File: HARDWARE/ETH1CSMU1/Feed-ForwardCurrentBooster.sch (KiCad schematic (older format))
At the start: 49 parts

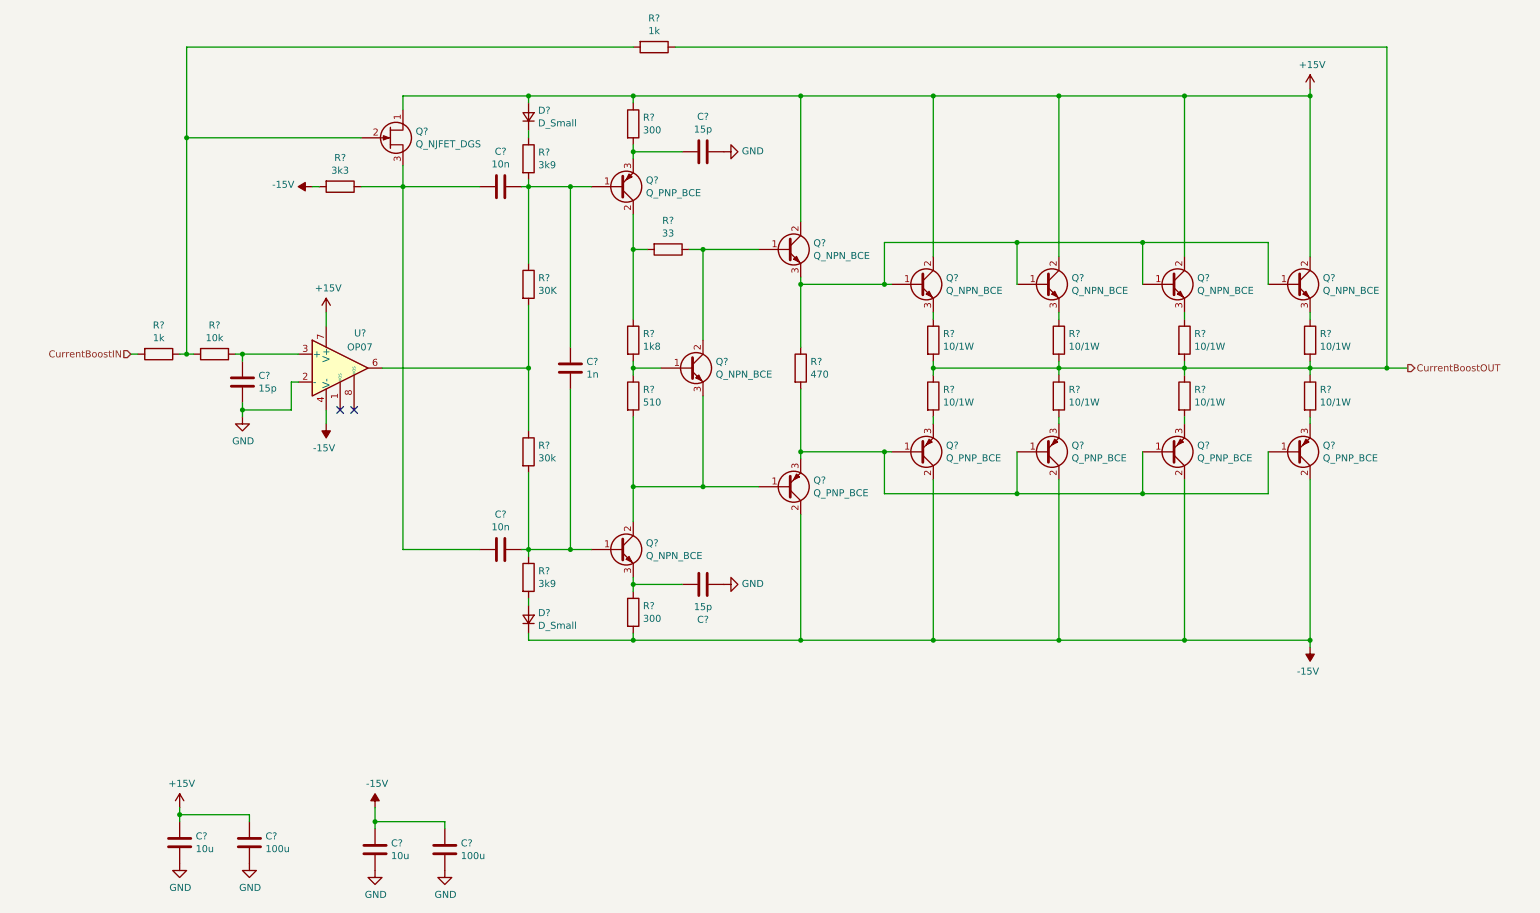
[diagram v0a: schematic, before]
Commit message: Added ADC
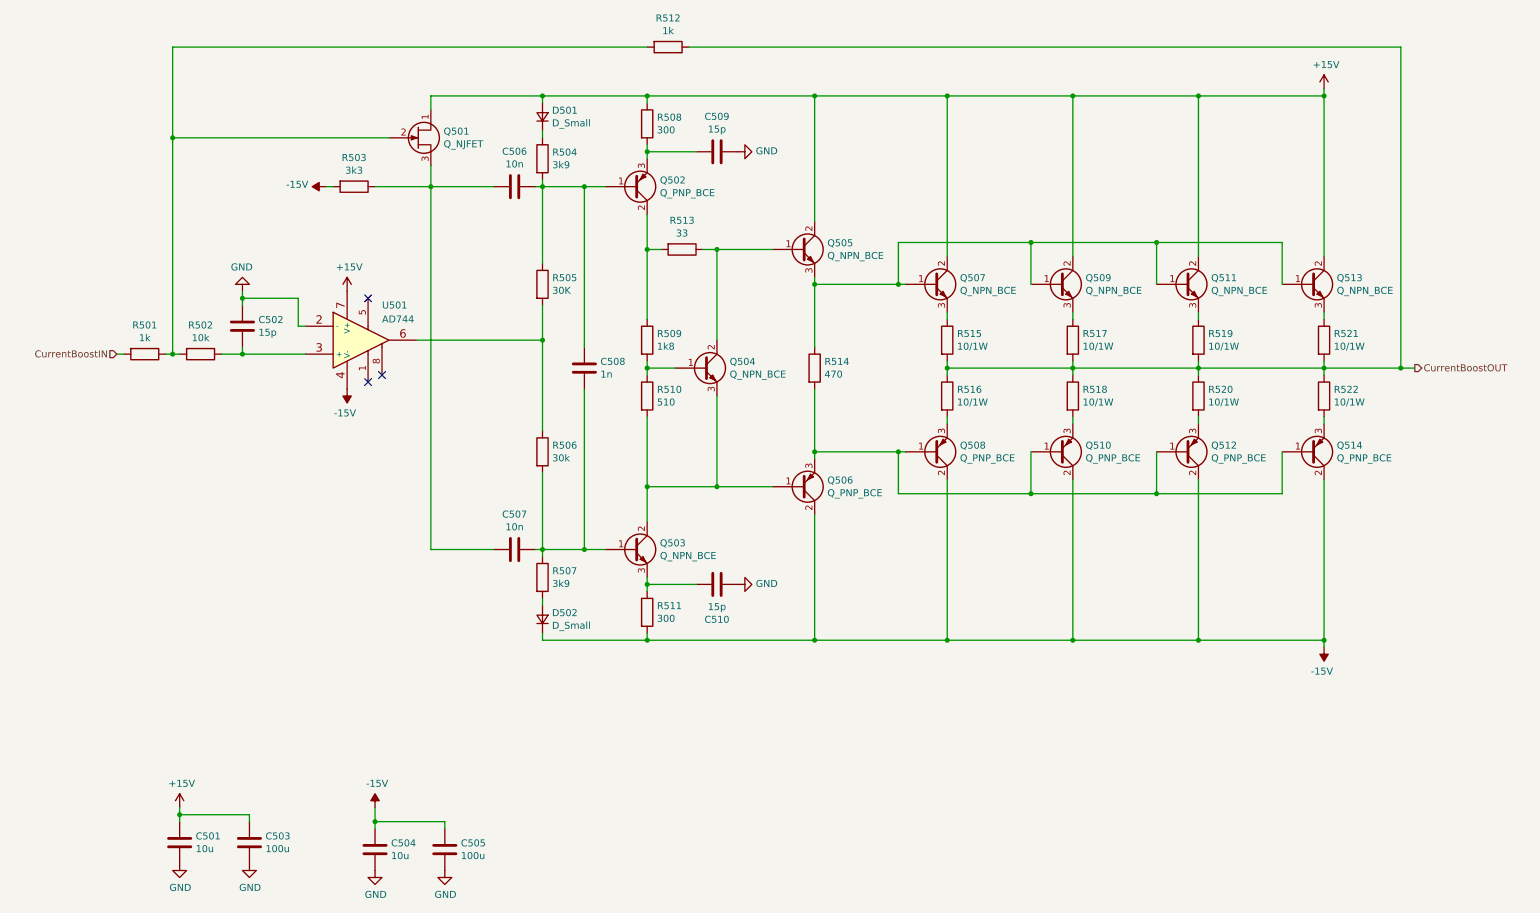
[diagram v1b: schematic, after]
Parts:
- removed U?: OP07, symbol Amplifier_Operational:OP07
- added U501: AD744, symbol opamp_local:AD744
- Q501: renamed from Q?; value Q_NJFET_DGS -> Q_NJFET
- gave numbers to parts that had none: 47
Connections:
- net +15V: now also U501.7 (V+)
- net -15V: now also U501.4 (V-)
- net GND: now also C502.1, U501.2 (-); no longer C502.2
- net at R505.2, R506.1: now also U501.6
- net at R502.1: now also C502.2, U501.3 (+); no longer C502.1
- no-connect marks 2 -> 3
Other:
- moved on the sheet: C502, C506, C507, C508, C509, C510, D501, D502, Q501, Q502, Q503, Q504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

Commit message: Commit
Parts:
- D501, D502: value D_Small -> 1N4148WS
- Q501: value Q_NJFET -> MMBF5486
- Q502, Q506: value Q_PNP_BCE -> MMBT200
- Q503, Q504, Q505: value Q_NPN_BCE -> SMBT2222
- Q507, Q509, Q511, Q513: value Q_NPN_BCE -> BCP56-16
- Q508, Q510, Q512, Q514: value Q_PNP_BCE -> BCP53
- R502: footprint (none) -> SMD:R_0603_Symbol1
- R515, R516, R517, R518, R519, R520, R521, R522: value 10/1W -> 10/2W
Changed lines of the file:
@@
 P 7100 3550
 F 0 "R515" H 7170 3596 50  0000 L CNN
-F 1 "10/1W" H 7170 3505 50  0000 L CNN
+F 1 "10/2W" H 7170 3505 50  0000 L CNN
 F 2 "" V 7030 3550 50  0001 C CNN
 F 3 "~" H 7100 3550 50  0001 C CNN
@@
 P 7100 3950
 F 0 "R516" H 7170 3996 50  0000 L CNN
-F 1 "10/1W" H 7170 3905 50  0000 L CNN
+F 1 "10/2W" H 7170 3905 50  0000 L CNN
 F 2 "" V 7030 3950 50  0001 C CNN
 F 3 "~" H 7100 3950 50  0001 C CNN
@@
 P 7000 3150
 F 0 "Q507" H 7191 3196 50  0000 L CNN
-F 1 "Q_NPN_BCE" H 7191 3105 50  0000 L CNN
+F 1 "BCP56-16" H 7191 3105 50  0000 L CNN
 F 2 "" H 7200 3250 50  0001 C CNN
 F 3 "~" H 7000 3150 50  0001 C CNN
@@
 P 6050 2900
 F 0 "Q505" H 6241 2946 50  0000 L CNN
-F 1 "Q_NPN_BCE" H 6241 2855 50  0000 L CNN
+F 1 "SMBT2222" H 6241 2855 50  0000 L CNN
 F 2 "" H 6250 3000 50  0001 C CNN
 F 3 "~" H 6050 2900 50  0001 C CNN
@@
 P 7000 4350
 F 0 "Q508" H 7191 4304 50  0000 L CNN
-F 1 "Q_PNP_BCE" H 7191 4395 50  0000 L CNN
+F 1 "BCP53" H 7191 4395 50  0000 L CNN
 F 2 "" H 7200 4450 50  0001 C CNN
 F 3 "~" H 7000 4350 50  0001 C CNN
@@
 P 6050 4600
 F 0 "Q506" H 6241 4554 50  0000 L CNN
-F 1 "Q_PNP_BCE" H 6241 4645 50  0000 L CNN
+F 1 "MMBT200" H 6241 4645 50  0000 L CNN
 F 2 "" H 6250 4700 50  0001 C CNN
 F 3 "~" H 6050 4600 50  0001 C CNN
@@
 P 5350 3750
 F 0 "Q504" H 5541 3796 50  0000 L CNN
-F 1 "Q_NPN_BCE" H 5541 3705 50  0000 L CNN
+F 1 "SMBT2222" H 5541 3705 50  0000 L CNN
 F 2 "" H 5550 3850 50  0001 C CNN
 F 3 "~" H 5350 3750 50  0001 C CNN
@@
 P 4850 5050
 F 0 "Q503" H 5041 5096 50  0000 L CNN
-F 1 "Q_NPN_BCE" H 5041 5005 50  0000 L CNN
+F 1 "SMBT2222" H 5041 5005 50  0000 L CNN
 F 2 "" H 5050 5150 50  0001 C CNN
 F 3 "~" H 4850 5050 50  0001 C CNN
@@
 P 4850 2450
 F 0 "Q502" H 5041 2404 50  0000 L CNN
-F 1 "Q_PNP_BCE" H 5041 2495 50  0000 L CNN
+F 1 "MMBT200" H 5041 2495 50  0000 L CNN
 F 2 "" H 5050 2550 50  0001 C CNN
 F 3 "~" H 4850 2450 50  0001 C CNN
@@
 P 4200 1950
 F 0 "D501" V 4246 1882 50  0000 R CNN
-F 1 "D_Small" V 4155 1882 50  0000 R CNN
+F 1 "1N4148WS" V 4155 1882 50  0000 R CNN
 F 2 "" V 4200 1950 50  0001 C CNN
 F 3 "~" V 4200 1950 50  0001 C CNN
@@
 P 4200 5550
 F 0 "D502" V 4246 5482 50  0000 R CNN
-F 1 "D_Small" V 4155 5482 50  0000 R CNN
+F 1 "1N4148WS" V 4155 5482 50  0000 R CNN
 F 2 "" V 4200 5550 50  0001 C CNN
 F 3 "~" V 4200 5550 50  0001 C CNN
@@
 P 3300 2100
 F 0 "Q501" H 3491 2146 50  0000 L CNN
-F 1 "Q_NJFET" H 3491 2055 50  0000 L CNN
+F 1 "MMBF5486" H 3491 2055 50  0000 L CNN
 F 2 "" H 3500 2200 50  0001 C CNN
 F 3 "~" H 3300 2100 50  0001 C CNN
@@
 F 0 "R502" V 1543 3650 50  0000 C CNN
 F 1 "10k" V 1634 3650 50  0000 C CNN
-F 2 "" V 1680 3650 50  0001 C CNN
+F 2 "SMD:R_0603_Symbol1" V 1680 3650 50  0001 C CNN
 F 3 "~" H 1750 3650 50  0001 C CNN
 	1    1750 3650
@@
 P 8000 3550
 F 0 "R517" H 8070 3596 50  0000 L CNN
-F 1 "10/1W" H 8070 3505 50  0000 L CNN
+F 1 "10/2W" H 8070 3505 50  0000 L CNN
 F 2 "" V 7930 3550 50  0001 C CNN
 F 3 "~" H 8000 3550 50  0001 C CNN
@@
 P 8000 3950
 F 0 "R518" H 8070 3996 50  0000 L CNN
-F 1 "10/1W" H 8070 3905 50  0000 L CNN
+F 1 "10/2W" H 8070 3905 50  0000 L CNN
 F 2 "" V 7930 3950 50  0001 C CNN
 F 3 "~" H 8000 3950 50  0001 C CNN
@@
 P 7900 3150
 F 0 "Q509" H 8091 3196 50  0000 L CNN
-F 1 "Q_NPN_BCE" H 8091 3105 50  0000 L CNN
+F 1 "BCP56-16" H 8091 3105 50  0000 L CNN
 F 2 "" H 8100 3250 50  0001 C CNN
 F 3 "~" H 7900 3150 50  0001 C CNN
@@
 P 7900 4350
 F 0 "Q510" H 8091 4304 50  0000 L CNN
-F 1 "Q_PNP_BCE" H 8091 4395 50  0000 L CNN
+F 1 "BCP53" H 8091 4395 50  0000 L CNN
 F 2 "" H 8100 4450 50  0001 C CNN
 F 3 "~" H 7900 4350 50  0001 C CNN
@@
 P 8900 3550
 F 0 "R519" H 8970 3596 50  0000 L CNN
-F 1 "10/1W" H 8970 3505 50  0000 L CNN
+F 1 "10/2W" H 8970 3505 50  0000 L CNN
 F 2 "" V 8830 3550 50  0001 C CNN
 F 3 "~" H 8900 3550 50  0001 C CNN
@@
 P 8900 3950
 F 0 "R520" H 8970 3996 50  0000 L CNN
-F 1 "10/1W" H 8970 3905 50  0000 L CNN
+F 1 "10/2W" H 8970 3905 50  0000 L CNN
 F 2 "" V 8830 3950 50  0001 C CNN
 F 3 "~" H 8900 3950 50  0001 C CNN
@@
 P 8800 3150
 F 0 "Q511" H 8991 3196 50  0000 L CNN
-F 1 "Q_NPN_BCE" H 8991 3105 50  0000 L CNN
+F 1 "BCP56-16" H 8991 3105 50  0000 L CNN
 F 2 "" H 9000 3250 50  0001 C CNN
 F 3 "~" H 8800 3150 50  0001 C CNN
@@
 P 8800 4350
 F 0 "Q512" H 8991 4304 50  0000 L CNN
-F 1 "Q_PNP_BCE" H 8991 4395 50  0000 L CNN
+F 1 "BCP53" H 8991 4395 50  0000 L CNN
 F 2 "" H 9000 4450 50  0001 C CNN
 F 3 "~" H 8800 4350 50  0001 C CNN
@@
 P 9800 3550
 F 0 "R521" H 9870 3596 50  0000 L CNN
-F 1 "10/1W" H 9870 3505 50  0000 L CNN
+F 1 "10/2W" H 9870 3505 50  0000 L CNN
 F 2 "" V 9730 3550 50  0001 C CNN
 F 3 "~" H 9800 3550 50  0001 C CNN
@@
 P 9800 3950
 F 0 "R522" H 9870 3996 50  0000 L CNN
-F 1 "10/1W" H 9870 3905 50  0000 L CNN
+F 1 "10/2W" H 9870 3905 50  0000 L CNN
 F 2 "" V 9730 3950 50  0001 C CNN
 F 3 "~" H 9800 3950 50  0001 C CNN
@@
 P 9700 3150
 F 0 "Q513" H 9891 3196 50  0000 L CNN
-F 1 "Q_NPN_BCE" H 9891 3105 50  0000 L CNN
+F 1 "BCP56-16" H 9891 3105 50  0000 L CNN
 F 2 "" H 9900 3250 50  0001 C CNN
 F 3 "~" H 9700 3150 50  0001 C CNN
@@
 P 9700 4350
 F 0 "Q514" H 9891 4304 50  0000 L CNN
-F 1 "Q_PNP_BCE" H 9891 4395 50  0000 L CNN
+F 1 "BCP53" H 9891 4395 50  0000 L CNN
 F 2 "" H 9900 4450 50  0001 C CNN
 F 3 "~" H 9700 4350 50  0001 C CNN
@@
 F 0 "U501" H 3050 3800 50  0000 L CNN
 F 1 "AD744" H 3050 3700 50  0000 L CNN
-F 2 "" H 2900 3550 60  0000 C CNN
+F 2 "" H 2900 3550 60  0001 C CNN
 F 3 "" H 2900 3550 60  0000 C CNN
 	1    2800 3550

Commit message: Footprints
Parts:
- removed C503, C505: 100u, symbol Device:C
- added C503, C505: 100u, symbol Device:CP
- C502, C509, C510: footprint (none) -> SMD:C_0603_Symbol5
- C506, C507: footprint (none) -> SMD:C_0603_Symbol2
- C508: footprint (none) -> Capacitors_SMD:C_0603
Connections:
- net +15V: now also C503.1
- net -15V: now also C505.2
- net GND: now also C503.2, C505.1
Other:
- moved on the sheet: C501
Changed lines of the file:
@@
 F 0 "C508" H 4615 3796 50  0000 L CNN
 F 1 "1n" H 4615 3705 50  0000 L CNN
-F 2 "" H 4538 3600 50  0001 C CNN
+F 2 "Capacitors_SMD:C_0603" H 4538 3600 50  0001 C CNN
 F 3 "~" H 4500 3750 50  0001 C CNN
 	1    4500 3750
@@
 F 0 "C509" V 5198 2200 50  0000 C CNN
 F 1 "15p" V 5289 2200 50  0000 C CNN
-F 2 "" H 5488 2050 50  0001 C CNN
+F 2 "SMD:C_0603_Symbol5" H 5488 2050 50  0001 C CNN
 F 3 "~" H 5450 2200 50  0001 C CNN
 	1    5450 2200
@@
 F 0 "C510" V 5198 5300 50  0000 C CNN
 F 1 "15p" V 5289 5300 50  0000 C CNN
-F 2 "" H 5488 5150 50  0001 C CNN
+F 2 "SMD:C_0603_Symbol5" H 5488 5150 50  0001 C CNN
 F 3 "~" H 5450 5300 50  0001 C CNN
 	1    5450 5300
@@
 F 0 "C507" V 3748 5050 50  0000 C CNN
 F 1 "10n" V 3839 5050 50  0000 C CNN
-F 2 "" H 4038 4900 50  0001 C CNN
+F 2 "SMD:C_0603_Symbol2" H 4038 4900 50  0001 C CNN
 F 3 "~" H 4000 5050 50  0001 C CNN
 	1    4000 5050
@@
 F 0 "C506" V 3748 2450 50  0000 C CNN
 F 1 "10n" V 3839 2450 50  0000 C CNN
-F 2 "" H 4038 2300 50  0001 C CNN
+F 2 "SMD:C_0603_Symbol2" H 4038 2300 50  0001 C CNN
 F 3 "~" H 4000 2450 50  0001 C CNN
 	1    4000 2450
@@
 L Device:C C501
 U 1 1 5BDC1227
-P 1600 7150
-F 0 "C501" H 1715 7196 50  0000 L CNN
-F 1 "10u" H 1715 7105 50  0000 L CNN
-F 2 "" H 1638 7000 50  0001 C CNN
-F 3 "~" H 1600 7150 50  0001 C CNN
-	1    1600 7150
-	1    0    0    -1
-$EndComp
-Wire Wire Line
-	1600 7000 1600 6950
+P 1600 7200
+F 0 "C501" H 1715 7246 50  0000 L CNN
+F 1 "10u" H 1715 7155 50  0000 L CNN
+F 2 "" H 1638 7050 50  0001 C CNN
+F 3 "~" H 1600 7200 50  0001 C CNN
+	1    1600 7200
+	1    0    0    -1
+$EndComp
+Wire Wire Line
+	1600 7050 1600 7000
 $Comp
 L power:GND #PWR0502
 U 1 1 5BDC3348
-P 1600 7300
-F 0 "#PWR0502" H 1600 7050 50  0001 C CNN
-F 1 "GND" H 1605 7127 50  0000 C CNN
-F 2 "" H 1600 7300 50  0001 C CNN
-F 3 "" H 1600 7300 50  0001 C CNN
-	1    1600 7300
-	1    0    0    -1
-$EndComp
-$Comp
-L Device:C C503
-U 1 1 5BDC38B6
-P 2100 7150
-F 0 "C503" H 2215 7196 50  0000 L CNN
-F 1 "100u" H 2215 7105 50  0000 L CNN
-F 2 "" H 2138 7000 50  0001 C CNN
-F 3 "~" H 2100 7150 50  0001 C CNN
-	1    2100 7150
+P 1600 7350
+F 0 "#PWR0502" H 1600 7100 50  0001 C CNN
+F 1 "GND" H 1605 7177 50  0000 C CNN
+F 2 "" H 1600 7350 50  0001 C CNN
+F 3 "" H 1600 7350 50  0001 C CNN
+	1    1600 7350
 	1    0    0    -1
 $EndComp
@@
 L power:GND #PWR0504
 U 1 1 5BDC3E2C
-P 2100 7300
-F 0 "#PWR0504" H 2100 7050 50  0001 C CNN
-F 1 "GND" H 2105 7127 50  0000 C CNN
-F 2 "" H 2100 7300 50  0001 C CNN
-F 3 "" H 2100 7300 50  0001 C CNN
-	1    2100 7300
-	1    0    0    -1
-$EndComp
-Wire Wire Line
-	2100 7000 2100 6950
-Wire Wire Line
-	2100 6950 1600 6950
+P 2100 7350
+F 0 "#PWR0504" H 2100 7100 50  0001 C CNN
+F 1 "GND" H 2105 7177 50  0000 C CNN
+F 2 "" H 2100 7350 50  0001 C CNN
+F 3 "" H 2100 7350 50  0001 C CNN
+	1    2100 7350
+	1    0    0    -1
+$EndComp
+Wire Wire Line
+	2100 7050 2100 7000
+Wire Wire Line
+	2100 7000 1600 7000
 $Comp
 L Device:C C504
@@
 F 3 "" H 3000 7350 50  0001 C CNN
 	1    3000 7350
-	1    0    0    -1
-$EndComp
-$Comp
-L Device:C C505
-U 1 1 5BDC638B
-P 3500 7200
-F 0 "C505" H 3615 7246 50  0000 L CNN
-F 1 "100u" H 3615 7155 50  0000 L CNN
-F 2 "" H 3538 7050 50  0001 C CNN
-F 3 "~" H 3500 7200 50  0001 C CNN
-	1    3500 7200
 	1    0    0    -1
 $EndComp
@@
 F 0 "C502" H 2165 3496 50  0000 L CNN
 F 1 "15p" H 2165 3405 50  0000 L CNN
-F 2 "" H 2088 3300 50  0001 C CNN
+F 2 "SMD:C_0603_Symbol5" H 2088 3300 50  0001 C CNN
 F 3 "~" H 2050 3450 50  0001 C CNN
 	1    2050 3450
@@
 L power:+15V #PWR0501
 U 1 1 5BE3B4B4
-P 1600 6900
-F 0 "#PWR0501" H 1600 6750 50  0001 C CNN
-F 1 "+15V" H 1615 7073 50  0000 C CNN
-F 2 "" H 1600 6900 50  0001 C CNN
-F 3 "" H 1600 6900 50  0001 C CNN
-	1    1600 6900
+P 1600 6950
+F 0 "#PWR0501" H 1600 6800 50  0001 C CNN
+F 1 "+15V" H 1615 7123 50  0000 C CNN
+F 2 "" H 1600 6950 50  0001 C CNN
+F 3 "" H 1600 6950 50  0001 C CNN
+	1    1600 6950
 	1    0    0    -1
 $EndComp
@@
 $EndComp
 Wire Wire Line
-	1600 6900 1600 6950
-Connection ~ 1600 6950
+	1600 6950 1600 7000
+Connection ~ 1600 7000
 Wire Wire Line
 	3000 6900 3000 7000
@@
 Wire Wire Line
 	1900 3650 2050 3650
+$Comp
+L Device:CP C503
+U 1 1 5C806E1C
+P 2100 7200
+F 0 "C503" H 2218 7246 50  0000 L CNN
+F 1 "100u" H 2218 7155 50  0000 L CNN
+F 2 "" H 2138 7050 50  0001 C CNN
+F 3 "~" H 2100 7200 50  0001 C CNN
+	1    2100 7200
+	1    0    0    -1
+$EndComp
+$Comp
+L Device:CP C505
+U 1 1 5C809259
+P 3500 7200
+F 0 "C505" H 3382 7154 50  0000 R CNN
+F 1 "100u" H 3382 7245 50  0000 R CNN
+F 2 "" H 3538 7050 50  0001 C CNN
+F 3 "~" H 3500 7200 50  0001 C CNN
+	1    3500 7200
+	-1   0    0    1
+$EndComp
 $EndSCHEMATC

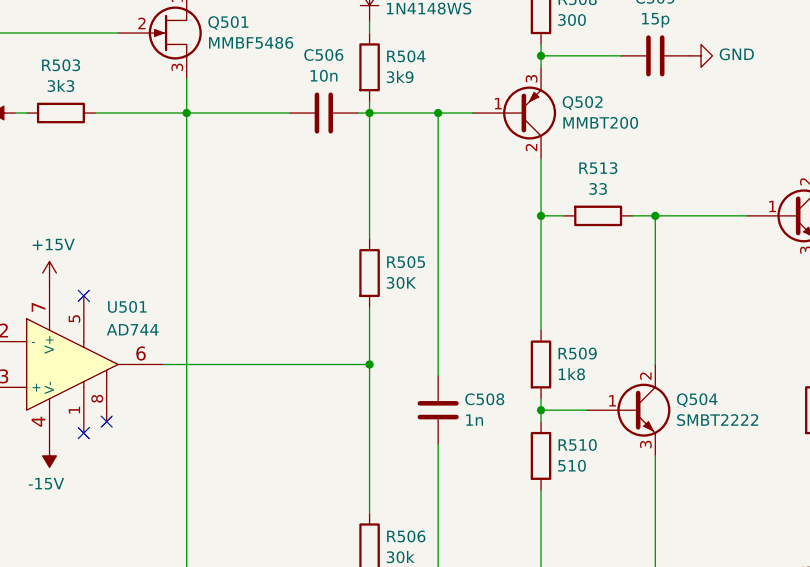
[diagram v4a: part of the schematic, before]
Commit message: Footprint selection
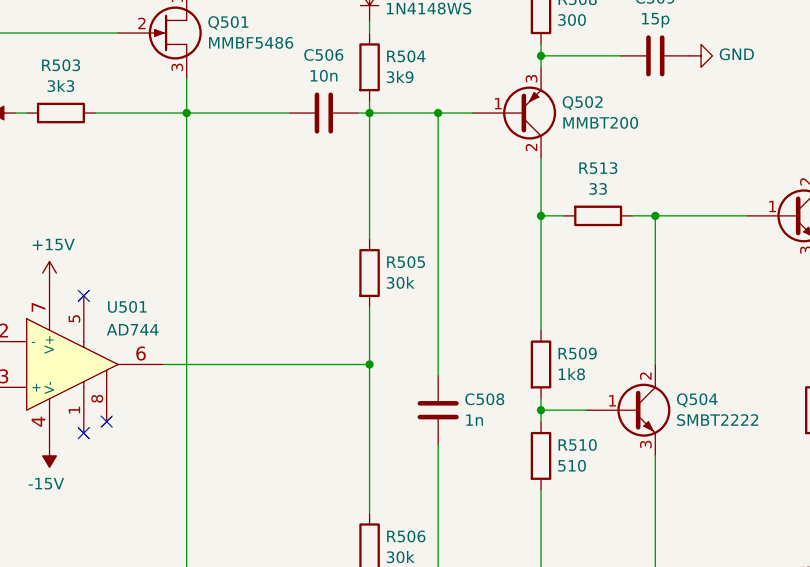
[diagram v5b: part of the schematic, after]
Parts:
- D501, D502: footprint (none) -> Diodes_SMD:D_SOD-323_HandSoldering
- R503, R508, R511: footprint (none) -> Resistors_SMD:R_0603
- R505: value 30K -> 30k; footprint (none) -> SMD:R_0603_Symbol7
- R506: footprint (none) -> SMD:R_0603_Symbol7
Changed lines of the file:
@@
 F 0 "R511" H 5020 5546 50  0000 L CNN
 F 1 "300" H 5020 5455 50  0000 L CNN
-F 2 "" V 4880 5500 50  0001 C CNN
+F 2 "Resistors_SMD:R_0603" V 4880 5500 50  0001 C CNN
 F 3 "~" H 4950 5500 50  0001 C CNN
 	1    4950 5500
@@
 F 0 "R508" H 5020 2046 50  0000 L CNN
 F 1 "300" H 5020 1955 50  0000 L CNN
-F 2 "" V 4880 2000 50  0001 C CNN
+F 2 "Resistors_SMD:R_0603" V 4880 2000 50  0001 C CNN
 F 3 "~" H 4950 2000 50  0001 C CNN
 	1    4950 2000
@@
 F 0 "D501" V 4246 1882 50  0000 R CNN
 F 1 "1N4148WS" V 4155 1882 50  0000 R CNN
-F 2 "" V 4200 1950 50  0001 C CNN
+F 2 "Diodes_SMD:D_SOD-323_HandSoldering" V 4200 1950 50  0001 C CNN
 F 3 "~" V 4200 1950 50  0001 C CNN
 	1    4200 1950
@@
 P 4200 3150
 F 0 "R505" H 4270 3196 50  0000 L CNN
-F 1 "30K" H 4270 3105 50  0000 L CNN
-F 2 "" V 4130 3150 50  0001 C CNN
+F 1 "30k" H 4270 3105 50  0000 L CNN
+F 2 "SMD:R_0603_Symbol7" V 4130 3150 50  0001 C CNN
 F 3 "~" H 4200 3150 50  0001 C CNN
 	1    4200 3150
@@
 F 0 "R506" H 4270 4396 50  0000 L CNN
 F 1 "30k" H 4270 4305 50  0000 L CNN
-F 2 "" V 4130 4350 50  0001 C CNN
+F 2 "SMD:R_0603_Symbol7" V 4130 4350 50  0001 C CNN
 F 3 "~" H 4200 4350 50  0001 C CNN
 	1    4200 4350
@@
 F 0 "D502" V 4246 5482 50  0000 R CNN
 F 1 "1N4148WS" V 4155 5482 50  0000 R CNN
-F 2 "" V 4200 5550 50  0001 C CNN
+F 2 "Diodes_SMD:D_SOD-323_HandSoldering" V 4200 5550 50  0001 C CNN
 F 3 "~" V 4200 5550 50  0001 C CNN
 	1    4200 5550
@@
 F 0 "R503" V 2643 2450 50  0000 C CNN
 F 1 "3k3" V 2734 2450 50  0000 C CNN
-F 2 "" V 2780 2450 50  0001 C CNN
+F 2 "Resistors_SMD:R_0603" V 2780 2450 50  0001 C CNN
 F 3 "~" H 2850 2450 50  0001 C CNN
 	1    2850 2450

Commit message: Redesigned feedback circuit.
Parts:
- R510, R514: footprint (none) -> Resistors_SMD:R_0603
- U501: footprint (none) -> Housings_SOIC:SOIC-8_3.9x4.9mm_Pitch1.27mm
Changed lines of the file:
@@
 F 0 "R514" H 6220 3796 50  0000 L CNN
 F 1 "470" H 6220 3705 50  0000 L CNN
-F 2 "" V 6080 3750 50  0001 C CNN
+F 2 "Resistors_SMD:R_0603" V 6080 3750 50  0001 C CNN
 F 3 "~" H 6150 3750 50  0001 C CNN
 	1    6150 3750
@@
 F 0 "R510" H 5020 3996 50  0000 L CNN
 F 1 "510" H 5020 3905 50  0000 L CNN
-F 2 "" V 4880 3950 50  0001 C CNN
+F 2 "Resistors_SMD:R_0603" V 4880 3950 50  0001 C CNN
 F 3 "~" H 4950 3950 50  0001 C CNN
 	1    4950 3950
@@
 F 0 "U501" H 3050 3800 50  0000 L CNN
 F 1 "AD744" H 3050 3700 50  0000 L CNN
-F 2 "" H 2900 3550 60  0001 C CNN
+F 2 "Housings_SOIC:SOIC-8_3.9x4.9mm_Pitch1.27mm" H 2900 3550 60  0001 C CNN
 F 3 "" H 2900 3550 60  0000 C CNN
 	1    2800 3550
